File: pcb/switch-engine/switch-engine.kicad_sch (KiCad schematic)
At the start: 1 part, among them U8 XILINX_ULTRASCALEPLUS_B676

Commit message: Continued initial schematic work on switch engine
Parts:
- removed U8: XILINX_ULTRASCALEPLUS_B676, symbol xilinx-azonenberg:XILINX_ULTRASCALEPLUS_B676
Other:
- added sheet RGMII PHY (rgmii.kicad_sch)
- added sheet Unused HPIO banks (unused-hpio.kicad_sch)
- sheet Line card interfaces ports: added 2V5, 3V3, GND; removed none
- sheet Power Supply ports: added 2V5; removed none
- sheet SFP28 interfaces ports: added 3V3, GND, GTY_VTT, I2C0_SCL, I2C0_SDA, I2C1_SCL, I2C1_SDA; removed none

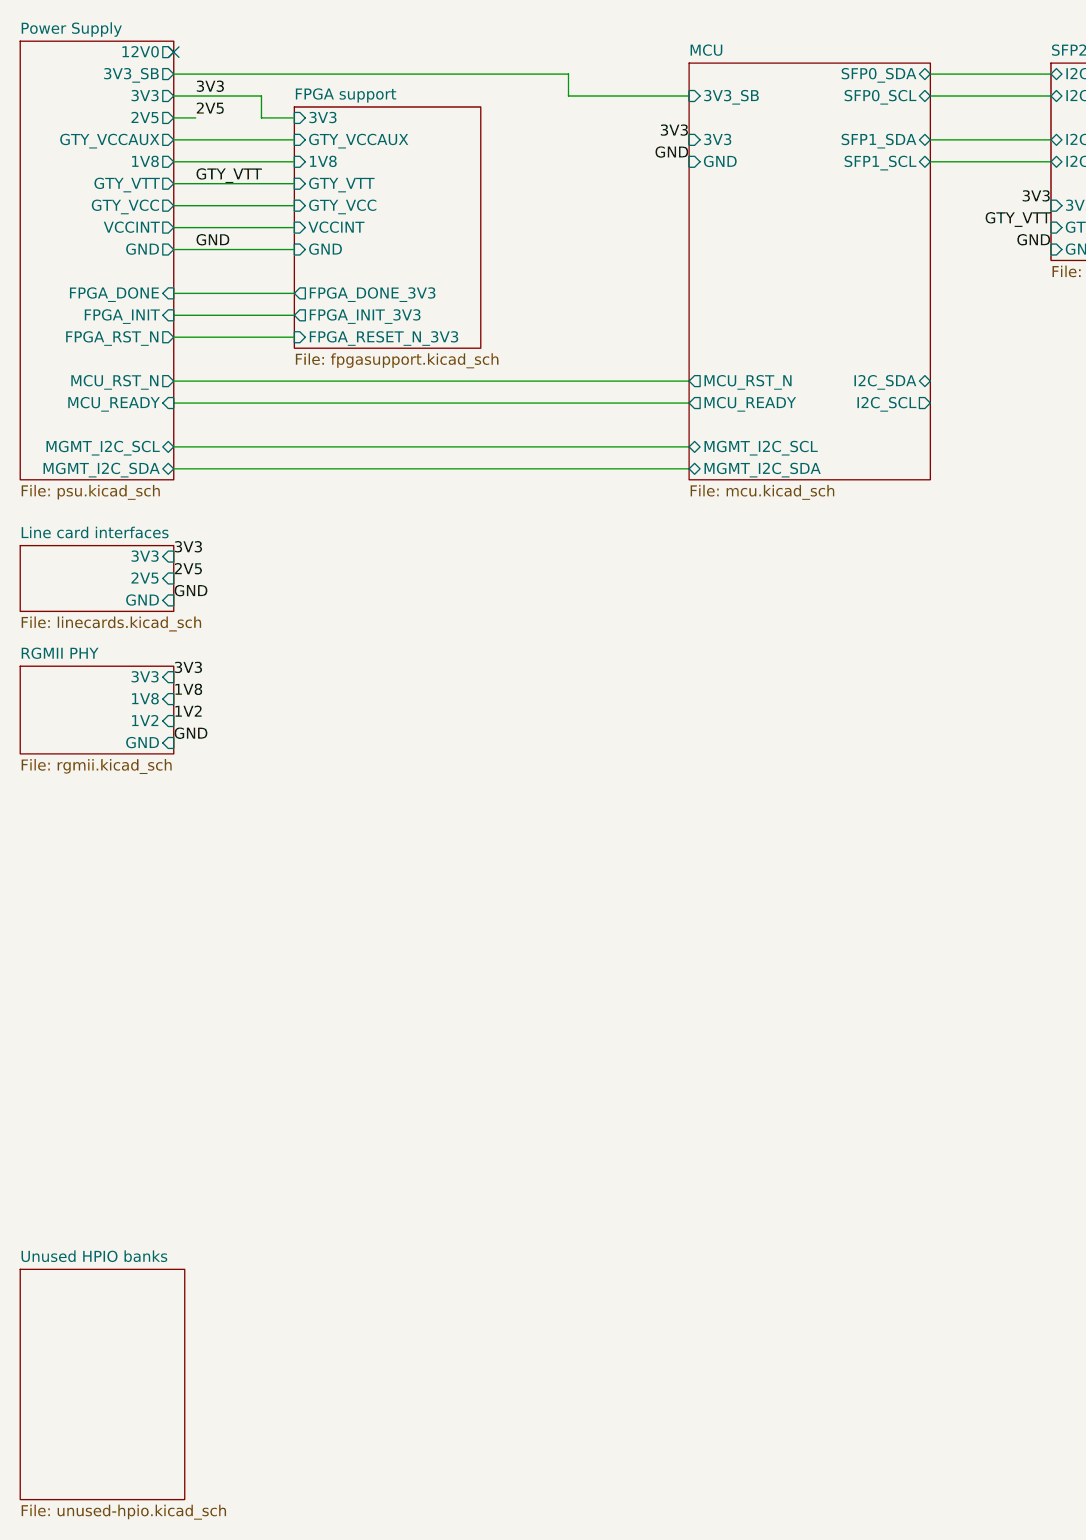
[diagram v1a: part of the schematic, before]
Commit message: First iteration of main board PCB schematic is now passing ERC
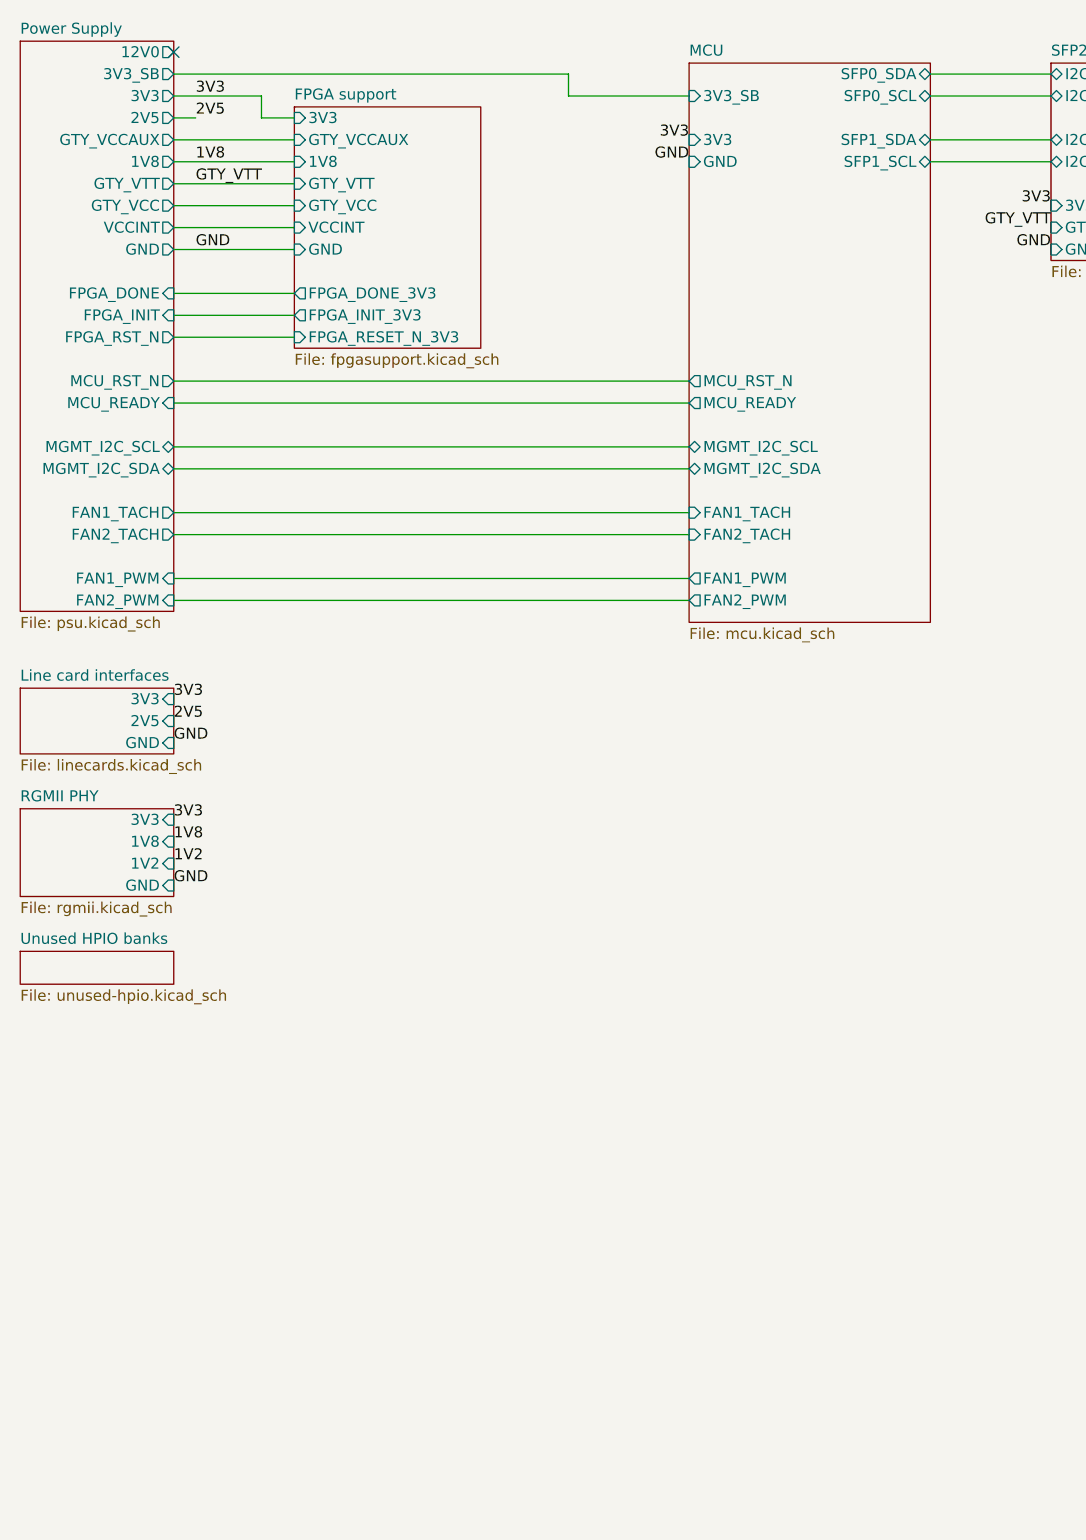
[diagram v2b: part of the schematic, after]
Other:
- sheet MCU ports: added FAN1_PWM, FAN1_TACH, FAN2_PWM, FAN2_TACH; removed I2C_SCL, I2C_SDA
- sheet Power Supply ports: added FAN1_PWM, FAN1_TACH, FAN2_PWM, FAN2_TACH; removed none
- company: (none) -> Antikernel Labs
- title: (none) -> LATENTRED Ethernet Switch - Main Board
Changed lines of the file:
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@@
 	(generator_version "8.0")
 	(paper "A4")
+	(title_block
+		(title "LATENTRED Ethernet Switch - Main Board")
+		(date "2025-06-02")
+		(rev "0.1")
+		(company "Antikernel Labs")
+		(comment 1 "Andrew D. Zonenberg")
+	)
 	(no_connect
 		(at 34.29 19.05)
@@
 	(wire
 		(pts
+			(xy 34.29 82.55) (xy 93.98 82.55)
+		)
+		(stroke
+			(width 0)
+			(type default)
+		)
+	)
+	(wire
+		(pts
 			(xy 80.01 21.59) (xy 80.01 24.13)
 		)
@@
 	(wire
 		(pts
+			(xy 34.29 80.01) (xy 93.98 80.01)
+		)
+		(stroke
+			(width 0)
+			(type default)
+		)
+	)
+	(wire
+		(pts
 			(xy 34.29 46.99) (xy 48.26 46.99)
 		)
@@
 	(wire
 		(pts
+			(xy 34.29 72.39) (xy 93.98 72.39)
+		)
+		(stroke
+			(width 0)
+			(type default)
+		)
+	)
+	(wire
+		(pts
 			(xy 34.29 31.75) (xy 48.26 31.75)
 		)
@@
 		(pts
 			(xy 44.45 26.67) (xy 48.26 26.67)
+		)
+		(stroke
+			(width 0)
+			(type default)
+		)
+	)
+	(wire
+		(pts
+			(xy 34.29 74.93) (xy 93.98 74.93)
 		)
 		(stroke
@@
 	)
 	(label "GND"
-		(at 34.29 99.06 0)
+		(at 34.29 115.57 0)
 		(fields_autoplaced yes)
 		(effects
@@
 		)
 	)
+	(label "1V8"
+		(at 36.83 31.75 0)
+		(fields_autoplaced yes)
+		(effects
+			(font
+				(size 1.27 1.27)
+			)
+			(justify left bottom)
+		)
+	)
 	(label "GND"
 		(at 93.98 31.75 180)
@@
 	)
 	(label "GND"
-		(at 34.29 82.55 0)
+		(at 34.29 99.06 0)
 		(fields_autoplaced yes)
 		(effects
@@
 	)
 	(label "1V8"
-		(at 34.29 93.98 0)
+		(at 34.29 110.49 0)
 		(fields_autoplaced yes)
 		(effects
@@
 	)
 	(label "2V5"
-		(at 34.29 80.01 0)
+		(at 34.29 96.52 0)
 		(fields_autoplaced yes)
 		(effects
@@
 	)
 	(label "1V2"
-		(at 34.29 96.52 0)
+		(at 34.29 113.03 0)
 		(fields_autoplaced yes)
 		(effects
@@
 	)
 	(label "3V3"
-		(at 34.29 91.44 0)
+		(at 34.29 107.95 0)
 		(fields_autoplaced yes)
 		(effects
@@
 	)
 	(label "3V3"
-		(at 34.29 77.47 0)
+		(at 34.29 93.98 0)
 		(fields_autoplaced yes)
 		(effects
@@
 	(sheet
 		(at 93.98 20.32)
-		(size 27.94 48.26)
+		(size 27.94 64.77)
 		(fields_autoplaced yes)
 		(stroke
@@
 		)
 		(property "Sheetfile" "mcu.kicad_sch"
-			(at 93.98 69.1646 0)
+			(at 93.98 85.6746 0)
 			(effects
 				(font
@@
 			)
 		)
-		(pin "I2C_SCL" output
-			(at 121.92 59.69 0)
-			(effects
-				(font
-					(size 1.27 1.27)
-				)
-				(justify right)
-			)
-		)
-		(pin "I2C_SDA" bidirectional
-			(at 121.92 57.15 0)
-			(effects
-				(font
-					(size 1.27 1.27)
-				)
-				(justify right)
-			)
-		)
 		(pin "MCU_READY" output
 			(at 93.98 59.69 180)
+			(effects
+				(font
+					(size 1.27 1.27)
+				)
+				(justify left)
+			)
+		)
+		(pin "FAN1_TACH" input
+			(at 93.98 72.39 180)
+			(effects
+				(font
+					(size 1.27 1.27)
+				)
+				(justify left)
+			)
+		)
+		(pin "FAN2_TACH" input
+			(at 93.98 74.93 180)
+			(effects
+				(font
+					(size 1.27 1.27)
+				)
+				(justify left)
+			)
+		)
+		(pin "FAN1_PWM" output
+			(at 93.98 80.01 180)
+			(effects
+				(font
+					(size 1.27 1.27)
+				)
+				(justify left)
+			)
+		)
+		(pin "FAN2_PWM" output
+			(at 93.98 82.55 180)
 			(effects
 				(font
@@
 	)
 	(sheet
-		(at 16.51 160.02)
-		(size 19.05 26.67)
+		(at 16.51 123.19)
+		(size 17.78 3.81)
 		(fields_autoplaced yes)
 		(stroke
@@
 		)
 		(property "Sheetname" "Unused HPIO banks"
-			(at 16.51 159.3084 0)
+			(at 16.51 122.4784 0)
 			(effects
 				(font
@@
 		)
 		(property "Sheetfile" "unused-hpio.kicad_sch"
-			(at 16.51 187.2746 0)
+			(at 16.51 127.5846 0)
 			(effects
 				(font
@@
 	(sheet
 		(at 16.51 17.78)
-		(size 17.78 50.8)
+		(size 17.78 66.04)
 		(fields_autoplaced yes)
 		(stroke
@@
 		)
 		(property "Sheetfile" "psu.kicad_sch"
-			(at 16.51 69.1646 0)
+			(at 16.51 84.4046 0)
 			(effects
 				(font
@@
 		(pin "2V5" output
 			(at 34.29 26.67 0)
+			(effects
+				(font
+					(size 1.27 1.27)
+				)
+				(justify right)
+			)
+		)
+		(pin "FAN2_TACH" output
+			(at 34.29 74.93 0)
+			(effects
+				(font
+					(size 1.27 1.27)
+				)
+				(justify right)
+			)
+		)
+		(pin "FAN1_TACH" output
+			(at 34.29 72.39 0)
+			(effects
+				(font
+					(size 1.27 1.27)
+				)
+				(justify right)
+			)
+		)
+		(pin "FAN1_PWM" input
+			(at 34.29 80.01 0)
+			(effects
+				(font
+					(size 1.27 1.27)
+				)
+				(justify right)
+			)
+		)
+		(pin "FAN2_PWM" input
+			(at 34.29 82.55 0)
 			(effects
 				(font
@@
 	)
 	(sheet
-		(at 16.51 76.2)
+		(at 16.51 92.71)
 		(size 17.78 7.62)
 		(fields_autoplaced yes)
@@
 		)
 		(property "Sheetname" "Line card interfaces"
-			(at 16.51 75.4884 0)
+			(at 16.51 91.9984 0)
 			(effects
 				(font
@@
 		)
 		(property "Sheetfile" "linecards.kicad_sch"
-			(at 16.51 84.4046 0)
+			(at 16.51 100.9146 0)
 			(effects
 				(font
@@
 		)
 		(pin "GND" input
-			(at 34.29 82.55 0)
+			(at 34.29 99.06 0)
 			(effects
 				(font
@@
 		)
 		(pin "3V3" input
-			(at 34.29 77.47 0)
+			(at 34.29 93.98 0)
 			(effects
 				(font
@@
 		)
 		(pin "2V5" input
-			(at 34.29 80.01 0)
+			(at 34.29 96.52 0)
 			(effects
 				(font
@@
 	)
 	(sheet
-		(at 16.51 90.17)
+		(at 16.51 106.68)
 		(size 17.78 10.16)
 		(fields_autoplaced yes)
@@
 		)
 		(property "Sheetname" "RGMII PHY"
-			(at 16.51 89.4584 0)
+			(at 16.51 105.9684 0)
 			(effects
 				(font
@@
 		)
 		(property "Sheetfile" "rgmii.kicad_sch"
-			(at 16.51 100.9146 0)
+			(at 16.51 117.4246 0)
 			(effects
 				(font
@@
 		)
 		(pin "GND" input
-			(at 34.29 99.06 0)
+			(at 34.29 115.57 0)
 			(effects
 				(font
@@
 		)
 		(pin "1V2" input
-			(at 34.29 96.52 0)
+			(at 34.29 113.03 0)
 			(effects
 				(font
@@
 		)
 		(pin "1V8" input
-			(at 34.29 93.98 0)
+			(at 34.29 110.49 0)
 			(effects
 				(font
@@
 		)
 		(pin "3V3" input
-			(at 34.29 91.44 0)
-			(effects
-				(font
+			(at 34.29 107.95 0)
+			(effects
+				(font

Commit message: Finished schematic review
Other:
- sheet FPGA support ports: added FPGA_INIT_OE; removed none
- sheet Power Supply ports: added FPGA_INIT_OE; removed none

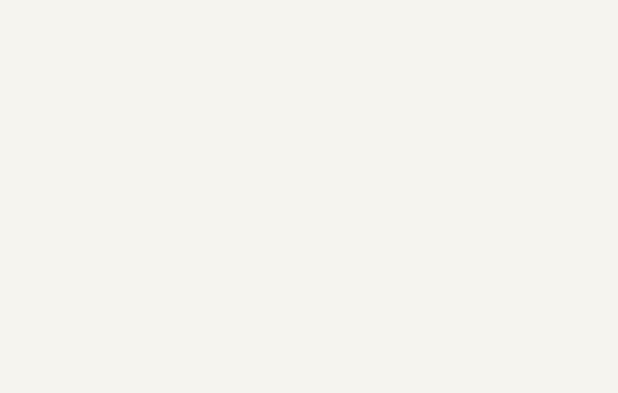
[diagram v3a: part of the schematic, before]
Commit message: Added footprints and created initial skeleton of layout
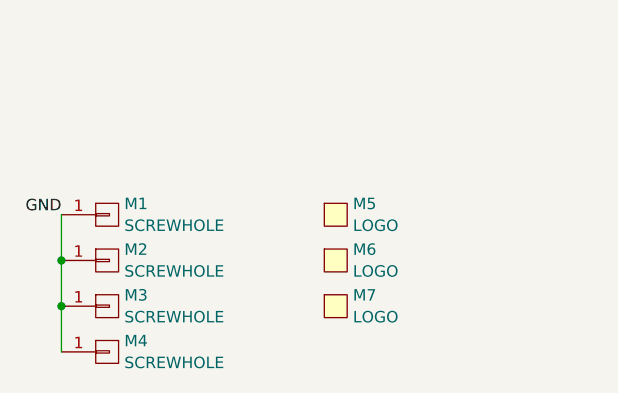
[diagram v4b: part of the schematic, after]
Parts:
- added M1, M2, M3, M4: SCREWHOLE, azonenberg_pcb:MECHANICAL_CLEARANCEHOLE_4_40, symbol conn:CONN_01X01
- added M5: LOGO, azonenberg_pcb:LONGTHING-1200DPI, symbol special-azonenberg:MECHANICAL
- added M6: LOGO, w_logo:Logo_silk_OSHW_6x6mm, symbol special-azonenberg:MECHANICAL
- added M7: LOGO, w_logo:Logo_silk_WEEE_3.4x5mm, symbol special-azonenberg:MECHANICAL
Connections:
- net GND: now also M1.1 (P1), M2.1 (P1), M3.1 (P1), M4.1 (P1)

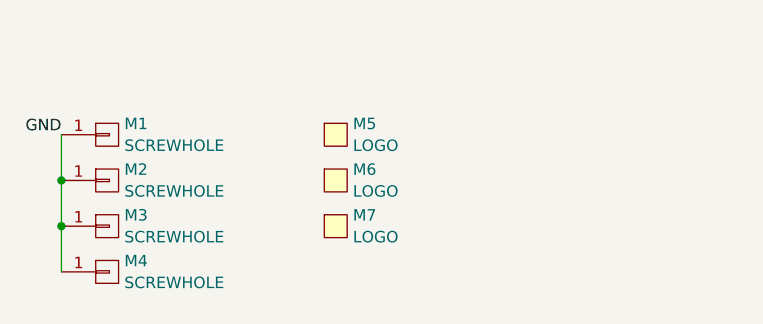
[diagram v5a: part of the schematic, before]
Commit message: Continued layout of MCU area, added cutout for fan
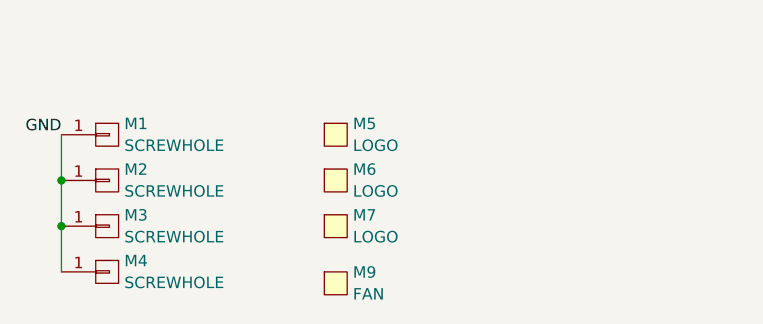
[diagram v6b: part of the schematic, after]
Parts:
- added M9: FAN, azonenberg_pcb:FAN_DELTA_EFB0412VHD-SP05, symbol special-azonenberg:MECHANICAL
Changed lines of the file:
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@@
 	(title_block
 		(title "LATENTRED Ethernet Switch - Main Board")
-		(date "2025-06-04")
+		(date "2025-06-06")
 		(rev "0.1")
 		(company "Antikernel Labs")
@@
 					(unit 1)
 				)
+			)
+		)
+	)
+	(symbol
+		(lib_id "special-azonenberg:MECHANICAL")
+		(at 49.53 184.15 0)
+		(unit 1)
+		(exclude_from_sim no)
+		(in_bom yes)
+		(on_board yes)
+		(dnp no)
+		(fields_autoplaced yes)
+		(property "Reference" "M9"
+			(at 52.705 182.9378 0)
+			(effects
+				(font
+					(size 1.27 1.27)
+				)
+				(justify left)
+			)
+		)
+		(property "Value" "FAN"
+			(at 52.705 185.3621 0)
+			(effects
+				(font
+					(size 1.27 1.27)
+				)
+				(justify left)
+			)
+		)
+		(property "Footprint" "azonenberg_pcb:FAN_DELTA_EFB0412VHD-SP05"
+			(at 49.53 184.15 0)
+			(effects
+				(font
+					(size 1.27 1.27)
+				)
+				(hide yes)
+			)
+		)
+		(property "Datasheet" ""
+			(at 49.53 184.15 0)
+			(effects
+				(font
+					(size 1.27 1.27)
+				)
+				(hide yes)
+			)
+		)
+		(property "Description" ""
+			(at 49.53 184.15 0)
+			(effects
+				(font
+					(size 1.27 1.27)
+				)
+				(hide yes)
+			)
+		)
+		(instances
+			(project ""
+				(path "/2594b26d-2fe5-4054-81d2-ca5df3747243"
+					(reference "M9")
+					(unit 1)
+				)

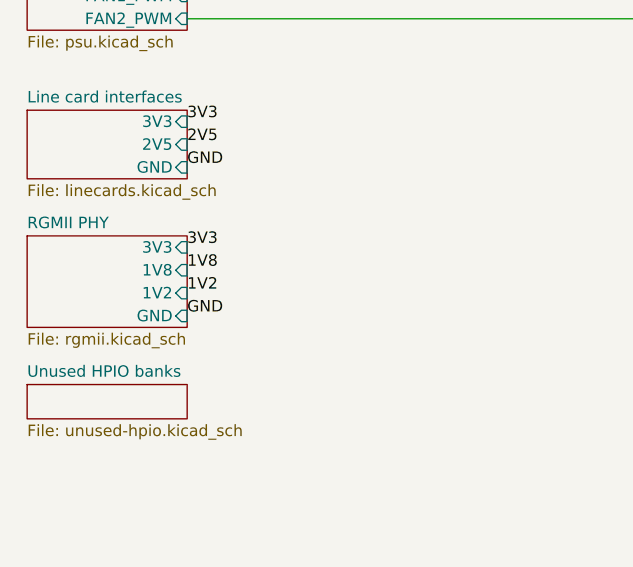
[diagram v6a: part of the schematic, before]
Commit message: More progress on PHY layout
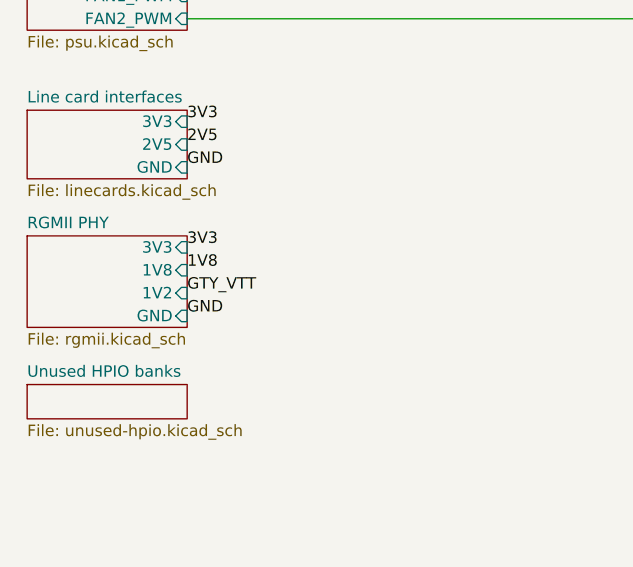
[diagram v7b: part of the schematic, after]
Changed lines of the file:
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@@
 		)
 	)
-	(label "1V2"
+	(label "GTY_VTT"
 		(at 34.29 115.57 0)
 		(fields_autoplaced yes)
